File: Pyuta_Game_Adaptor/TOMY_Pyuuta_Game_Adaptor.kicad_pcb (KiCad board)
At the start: 2 copper layers, 45.5 x 76.5 mm, 7 parts, among them J1 Tomy Pyūta I/O Port, J2 Tomy Pyūta Cartridge

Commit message: Initial design completed
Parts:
- moved C1 6.15 mm to (44.0, 41.7)
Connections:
- J1 pad 21: unconnected-(J1-~{MEMEN}-Pad21) -> /~{MEMEN}
- J1 pad 31: unconnected-(J1-~{WE}-Pad31) -> /~{WE}
- J1 pad 37: unconnected-(J1-~{RESET}-Pad37) -> /~{RESET}
- J1 pad 50: /V_{CC} -> unconnected-(J1-V_{CC}-Pad50)
- J2 pad 21: unconnected-(J2-~{CROM1}-Pad21) -> /~{MEMEN}
- J2 pad 32: unconnected-(J2-~{WE}-Pad32) -> /~{WE}
- J2 pad 4: unconnected-(J2-~{RESET}-Pad4) -> /~{RESET}
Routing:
- net /GND: track 34.1 -> 107.1 mm, vias 0 -> 10
- net /~{RESET}: track 0.00 -> 44.6 mm
- net /~{MEMEN}: track 0.00 -> 30.3 mm, vias 0 -> 1
- net /~{WE}: track 0.00 -> 25.4 mm, vias 0 -> 1
- net /V_{CC}: track 63.1 -> 60.3 mm
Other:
- outline, holes or cut-outs redrawn
- board text added: "100µF"
- board text added: "Tomy Pyūta 32KB Cartridge"
- board text added: "↓ Cartridge Front ↓"

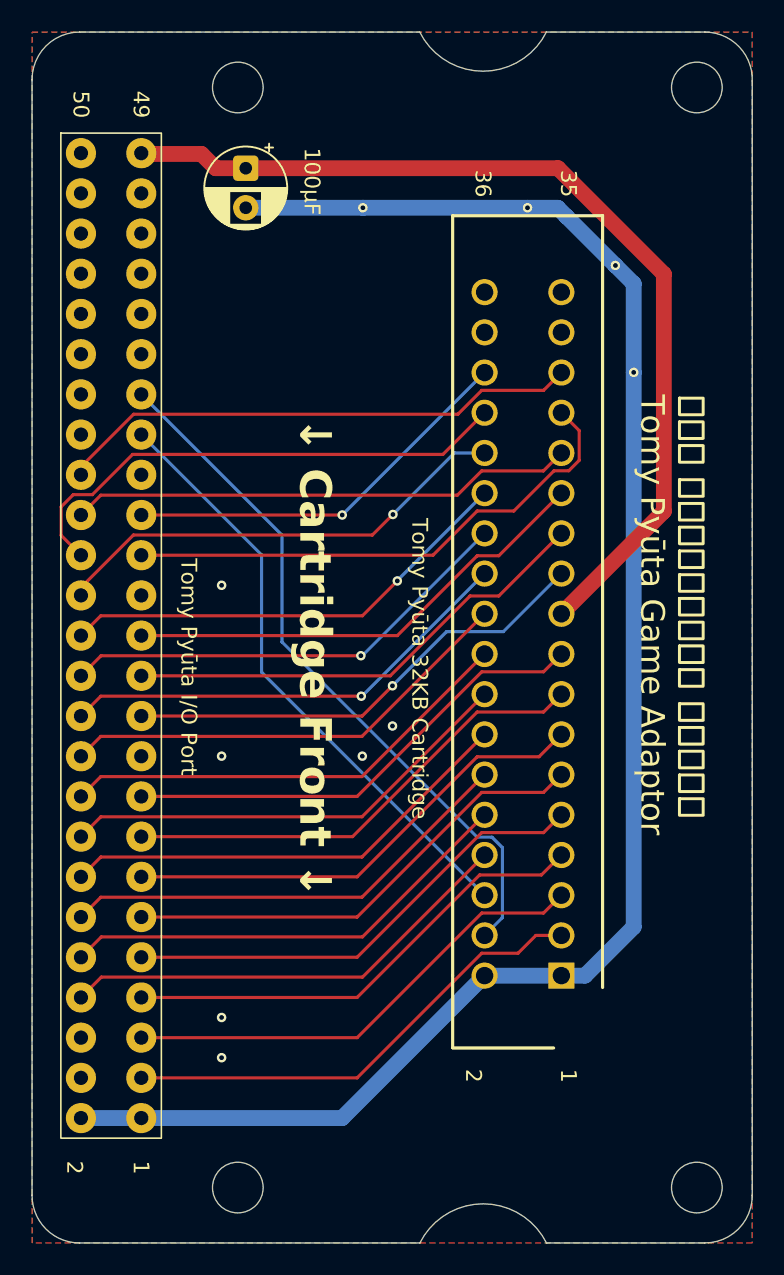
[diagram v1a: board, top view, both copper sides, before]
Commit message: Added info about unused parts to schematic
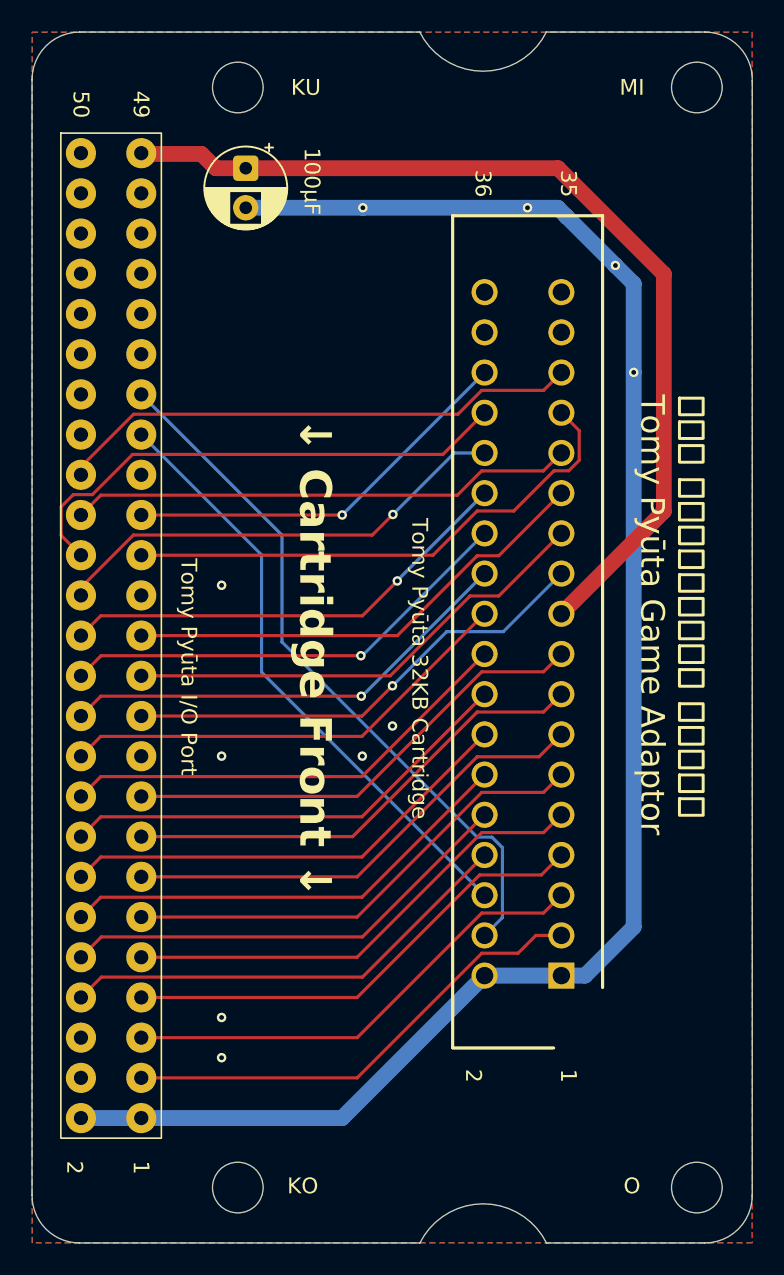
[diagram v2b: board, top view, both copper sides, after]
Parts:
- H1: value MountingHole -> KU
- H2: value MountingHole -> MI
- H3: value MountingHole -> O
- H4: value MountingHole -> KO
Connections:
- J1 pad 48: unconnected-(J1-KILLROM-Pad48) -> /KILLROM
- J2 pad 35: unconnected-(J2-~{CROM0}-Pad35) -> /~{CROM0}
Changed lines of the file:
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@@
 	(net 41 "unconnected-(J1-~{IAQ}-Pad47)")
 	(net 42 "unconnected-(J1-~{EXP1}-Pad39)")
-	(net 43 "unconnected-(J1-KILLROM-Pad48)")
+	(net 43 "/KILLROM")
 	(net 44 "unconnected-(J1-~{EXP2}-Pad40)")
 	(net 45 "unconnected-(J1-~{IOPORT}-Pad19)")
@@
 	(net 48 "unconnected-(J1-~{EXM00}-Pad42)")
 	(net 49 "unconnected-(J1-~{EXP3}-Pad41)")
-	(net 50 "unconnected-(J2-~{CROM0}-Pad35)")
+	(net 50 "/~{CROM0}")
 	(net 51 "unconnected-(J2-~{INT4}-Pad34)")
 	(net 52 "unconnected-(J2-SOUND-Pad33)")
@@
 			(layers "*.Cu" "*.Mask")
 			(remove_unused_layers no)
-			(net 50 "unconnected-(J2-~{CROM0}-Pad35)")
+			(net 50 "/~{CROM0}")
 			(pinfunction "~{CROM0}")
-			(pintype "passive+no_connect")
+			(pintype "passive")
 		)
 		(pad "36" thru_hole circle
@@
 			(layers "*.Cu" "*.Mask")
 			(remove_unused_layers no)
-			(net 43 "unconnected-(J1-KILLROM-Pad48)")
+			(net 43 "/KILLROM")
 			(pinfunction "KILLROM")
-			(pintype "passive+no_connect")
+			(pintype "passive")
 		)
 		(pad "49" thru_hole circle
@@
 			)
 		)
-		(property "Value" "MountingHole"
-			(at 0 3.75 0)
-			(layer "F.Fab")
-			(hide yes)
+		(property "Value" "KO"
+			(at 4.101627 -0.099994 180)
+			(layer "F.SilkS")
 			(effects
 				(font
@@
 			)
 		)
-		(property "Value" "MountingHole"
-			(at 0 3.75 0)
-			(layer "F.Fab")
-			(hide yes)
+		(property "Value" "O"
+			(at -4.098373 -0.099994 0)
+			(layer "F.SilkS")
 			(effects
 				(font
@@
 			)
 		)
-		(property "Value" "MountingHole"
-			(at 0 3.75 0)
-			(layer "F.Fab")
-			(hide yes)
+		(property "Value" "KU"
+			(at 4.301627 0 0)
+			(layer "F.SilkS")
 			(effects
 				(font
@@
 			)
 		)
-		(property "Value" "MountingHole"
-			(at 0 3.75 0)
-			(layer "F.Fab")
-			(hide yes)
-			(effects
-				(font
+		(property "Value" "MI"
+			(at -4.098373 0.000006 0)
+			(layer "F.SilkS")
+			(effects
+				(font
